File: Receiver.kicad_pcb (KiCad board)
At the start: 2 copper layers, 30 x 30 mm, 25 parts, among them U1 TL074 (ggf. durch TLV4172IPWR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

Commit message: Update schematic and pcb
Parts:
- added D3: LED, LEDs:LED_0603, F.Cu at (127.5, 118.5)
- added D4: LED, LEDs:LED_0603, F.Cu at (90.0, 119.0)
- added J1: +12V, optoreceiver:Hirschmann_MST201, F.Cu at (127.5, 127.5)
- added J2: -12V, optoreceiver:Hirschmann_MST201, F.Cu at (90.0, 127.5)
- added J3: GND, optoreceiver:Hirschmann_MST201, F.Cu at (90.0, 90.0)
- added J4: OUTPUT, optoreceiver:Hirschmann_MST201, F.Cu at (127.5, 90.0)
- added J5: Conn_01x04, Pin_Headers:Pin_Header_Straight_1x04_Pitch2.54mm, F.Cu at (113.0, 127.5)
- added R13: 1k, Resistors_SMD:R_0603, F.Cu at (127.5, 122.0)
- added R14: 1k, Resistors_SMD:R_0603, F.Cu at (90.0, 122.3)
- D2: value Schottky -> BAT54; footprint Diode_SMD:D_SOD-123 -> Diodes_SMD:D_SOT-23_ANK
- moved C1 33.0 mm to (108.5, 107.5)
- moved D2 25.9 mm to (123.0, 113.0)
- moved C2 25.0 mm to (108.5, 104.5)
- moved RV2 20.5 mm to (120.0, 103.0)
- moved D1 19.8 mm to (112.0, 94.5)
- moved RV1 18.5 mm to (99.0, 103.0)
- moved C3 18.2 mm to (102.5, 115.5)
- moved C4 18.2 mm to (102.5, 113.5)
- moved C5 18.2 mm to (114.8, 113.5)
- moved C6 18.2 mm to (114.8, 115.5)
- moved C7 18.2 mm to (114.8, 108.5)
- moved C8 18.2 mm to (119.2, 108.5)
- moved R1 18.2 mm to (99.5, 109.5)
- moved R10 18.2 mm to (116.5, 112.8)
- moved R11 18.2 mm to (116.5, 110.8)
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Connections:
- net Net-(C8-Pad2) renamed /OUTPUT
- U1 pad 4: Net-(U1-Pad4) -> +12V
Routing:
- net Net-(C4-Pad1): track 5.45 -> 0.00 mm
- net Net-(R4-Pad1): track 5.43 -> 0.00 mm
- net Net-(R1-Pad2): track 5.18 -> 0.00 mm
- net Net-(C3-Pad1): track 2.36 -> 0.00 mm, vias 1 -> 0
- added copper zone on B.Cu, net GND
- added copper zone on F.Cu, net GND
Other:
- board size 30 x 30 mm -> 43.5 x 43.5 mm
- board text added: "+12 V"
- board text added: "-12 V"
- board text added: "GND"
- board text added: "OUTPUT"

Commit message: Add files via upload
- Platzierung und Silkscreen angepasst
- 3D Modelle ergänzt
- aktuelle Renderbilder erzeugt
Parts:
- C1, C2, R1, R10, R13, R14, R2, R3, R9: moved to B.Cu
- C5, C6: moved to F.Cu
- D1: footprint kicadlibs:Osram_DIL2_4.3x4.65mm_P5.08mm -> OptoDevice:Osram_SMD2_4.3x4.65mm_P5.08mm
- RV1, RV2: footprint SparkFun-Electromechanical:TRIM_POT -> User-Submitted:BOURNS-3362P_pot
- U1: footprint Package_SO:TSSOP-14_4.4x5mm_P0.65mm -> Package_SO:SOIC-14_3.9x8.7mm_P1.27mm
- moved R6 10.9 mm to (117.0, 117.0)
- moved C7 9.10 mm to (123.5, 111.0), turned to 0 degrees
- moved C2 7.50 mm to (108.5, 112.0)
- moved D1 4.61 mm to (111.0, 90.0)
- moved D3 4.30 mm to (127.5, 122.8), turned to 90 degrees
- moved D4 3.90 mm to (90.0, 122.9), turned to 270 degrees
- moved R5 3.73 mm to (99.5, 116.0)
- moved C8 3.58 mm to (116.0, 107.0), turned to 0 degrees
- moved C3 3.04 mm to (99.5, 116.0)
- moved C4 3.04 mm to (99.5, 113.0)
- moved C6 3.01 mm to (117.0, 113.5), turned to 0 degrees
- moved R8 3.01 mm to (114.5, 114.5), turned to 270 degrees
- moved C5 2.85 mm to (117.0, 115.2), turned to 0 degrees
- moved RV2 2.83 mm to (118.0, 101.0), turned to 0 degrees
- moved R2 2.69 mm to (97.0, 114.5), turned to 270 degrees
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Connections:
- U1 pad 11: Net-(U1-Pad11) -> -12V
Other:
- outline, holes or cut-outs redrawn
- board text added: "+12V"
- board text added: "-12V"
- board text added: "Bandpass Stufe 1"
- board text added: "Bandpass Stufe 2"
- board text added: "Gleichrichter"
- board text added: "NEG PWR"
- board text added: "OUT"
- board text added: "OptoReceiver V0.1"
- board text added: "POS PWR"
- board text added: "Transimpedanz Verstärker"
- board text added: "Verstärker Endstufe"

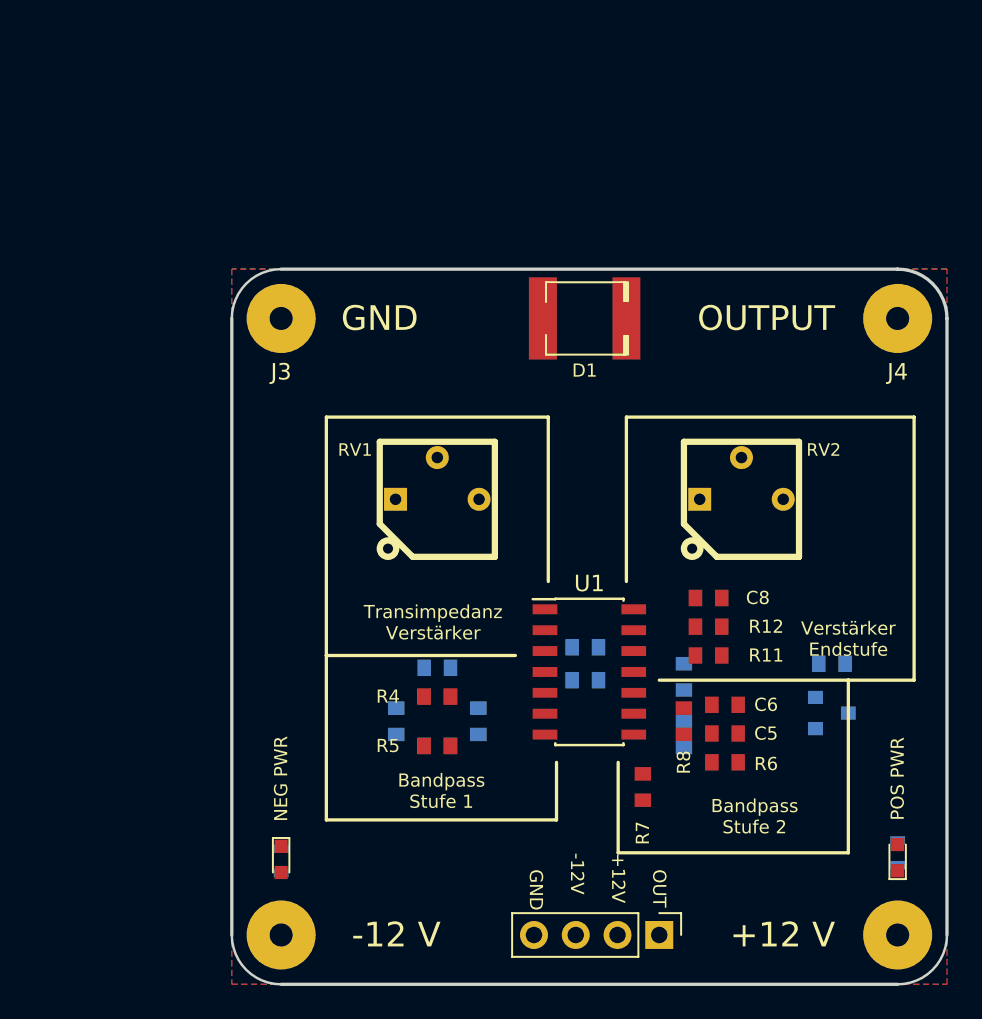
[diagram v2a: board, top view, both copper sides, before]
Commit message: PCB auf Rastermaß angepasst
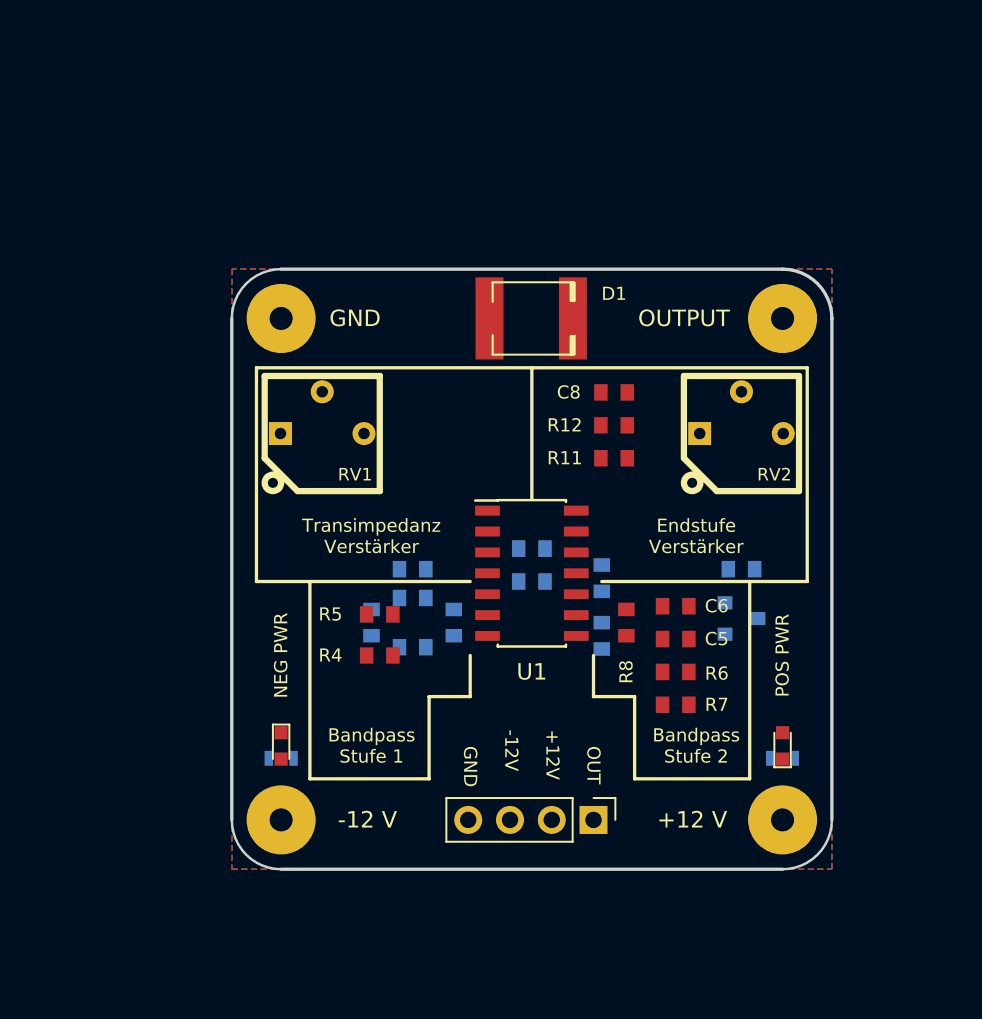
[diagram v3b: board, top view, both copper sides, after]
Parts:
- moved C8 13.8 mm to (110.2, 94.5)
- moved R12 13.5 mm to (110.2, 96.5)
- moved R11 13.3 mm to (110.2, 98.5), turned to 180 degrees
- moved J1 9.90 mm to (120.5, 120.5)
- moved D3 9.76 mm to (120.5, 116.0)
- moved R13 9.06 mm to (120.5, 116.8), turned to 180 degrees
- moved R5 8.73 mm to (96.0, 108.0), turned to 180 degrees
- moved J5 8.06 mm to (109.0, 120.5)
- moved RV1 8.06 mm to (92.5, 97.0)
- moved C7 7.96 mm to (118.0, 105.2)
- moved D2 7.96 mm to (118.0, 108.2)
- moved R10 7.81 mm to (109.5, 105.8)
- moved R9 7.81 mm to (109.5, 109.3)
- moved J2 7.00 mm to (90.0, 120.5)
- moved J4 7.00 mm to (120.5, 90.0)
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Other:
- board size 43.5 x 43.5 mm -> 36.5 x 36.5 mm
- board text added: "Endstufe Verstärker"
- board text added: "OptoReceiver V0.2"
- board text added: "Thomas Gatzweiler"
- board text added: "Tobias Cronenbroeck"
- board text removed: "OptoReceiver V0.1"
- board text removed: "Verstärker Endstufe"

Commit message: Routing + Render Bilder erneuert
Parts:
- moved J5 1.50 mm to (109.0, 119.0)
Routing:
- net +12V: track 0.00 -> 53.9 mm, vias 0 -> 2
- net /OUTPUT: track 0.00 -> 53.6 mm
- net -12V: track 0.00 -> 39.6 mm, vias 0 -> 2
- net Net-(D1-Pad2): track 0.00 -> 27.5 mm
- net Net-(C3-Pad1): track 0.00 -> 20.3 mm, vias 0 -> 1
- net Net-(R1-Pad2): track 0.00 -> 19.1 mm, vias 0 -> 1
- net Net-(C7-Pad2): track 0.00 -> 17.0 mm, vias 0 -> 1
- net Net-(R11-Pad1): track 0.00 -> 16.3 mm
- net Net-(C5-Pad1): track 0.00 -> 13.2 mm, vias 0 -> 1
- net Net-(R12-Pad1): track 0.00 -> 12.7 mm, vias 0 -> 1
- net Net-(R4-Pad1): track 0.00 -> 12.2 mm
- net Net-(R10-Pad2): track 0.00 -> 6.72 mm, vias 0 -> 1
- net Net-(C3-Pad2): track 0.00 -> 6.66 mm
- net Net-(C5-Pad2): track 0.00 -> 6.00 mm
- net Net-(C6-Pad1): track 0.00 -> 5.47 mm
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
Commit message: Real Value Simulation + Update in Schematic
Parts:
- C3, C4: value 390p -> 750p
- C5, C6: value 390p -> 820p
- R1: value 75K -> 24K
- R10: value 274 -> 360
- R2: value 1K02 -> 1K
- R3: value 102K -> 100K
- R4: value 15K4 -> 22K
- R5: value 249 -> 360
- R6: value 49K9 -> 24K
- R7: value 976 -> 1K
- R8: value 97K6 -> 100K
- R9: value 15K -> 22K
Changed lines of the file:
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@@
     (35 F.Paste user)
     (36 B.SilkS user)
-    (37 F.SilkS user)
+    (37 F.SilkS user hide)
     (38 B.Mask user)
-    (39 F.Mask user)
+    (39 F.Mask user hide)
     (40 Dwgs.User user)
     (41 Cmts.User user)
@@
     (45 Margin user)
     (46 B.CrtYd user)
-    (47 F.CrtYd user)
+    (47 F.CrtYd user hide)
     (48 B.Fab user)
-    (49 F.Fab user)
+    (49 F.Fab user hide)
   )
   (setup
-    (last_trace_width 0.5)
+    (last_trace_width 0.25)
     (user_trace_width 0.3)
     (user_trace_width 0.5)
@@
       (effects (font (size 0.8 0.8) (thickness 0.15)) (justify mirror))
     )
-    (fp_text value 390p (at 0 -1.45 180) (layer B.Fab)
+    (fp_text value 750p (at 0 -1.45 180) (layer B.Fab)
       (effects (font (size 0.8 0.8) (thickness 0.15)) (justify mirror))
     )
@@
       (effects (font (size 0.8 0.8) (thickness 0.15)) (justify mirror))
     )
-    (fp_text value 390p (at 0 -1.45 180) (layer B.Fab)
+    (fp_text value 750p (at 0 -1.45 180) (layer B.Fab)
       (effects (font (size 0.8 0.8) (thickness 0.15)) (justify mirror))
     )
@@
       (effects (font (size 0.8 0.8) (thickness 0.15)))
     )
-    (fp_text value 390p (at 0 1.45) (layer F.Fab)
+    (fp_text value 820p (at 0 1.45) (layer F.Fab)
       (effects (font (size 0.8 0.8) (thickness 0.15)))
     )
@@
       (effects (font (size 0.8 0.8) (thickness 0.15)))
     )
-    (fp_text value 390p (at 0 1.45) (layer F.Fab)
+    (fp_text value 820p (at 0 1.45) (layer F.Fab)
       (effects (font (size 0.8 0.8) (thickness 0.15)))
     )
@@
       (effects (font (size 0.8 0.8) (thickness 0.15)) (justify mirror))
     )
-    (fp_text value 75K (at 0 -1.45) (layer B.Fab)
+    (fp_text value 24K (at 0 -1.45) (layer B.Fab)
       (effects (font (size 0.8 0.8) (thickness 0.15)) (justify mirror))
     )
@@
       (effects (font (size 0.8 0.8) (thickness 0.15)) (justify mirror))
     )
-    (fp_text value 1K02 (at 0 -1.45 270) (layer B.Fab)
+    (fp_text value 1K (at 0 -1.45 270) (layer B.Fab)
       (effects (font (size 0.8 0.8) (thickness 0.15)) (justify mirror))
     )
@@
       (effects (font (size 0.8 0.8) (thickness 0.15)) (justify mirror))
     )
-    (fp_text value 102K (at 0 -1.45 270) (layer B.Fab)
+    (fp_text value 100K (at 0 -1.45 270) (layer B.Fab)
       (effects (font (size 0.8 0.8) (thickness 0.15)) (justify mirror))
     )
@@
       (effects (font (size 0.8 0.8) (thickness 0.15)))
     )
-    (fp_text value 15K4 (at 0 1.45) (layer F.Fab)
+    (fp_text value 22K (at 0 1.45) (layer F.Fab)
       (effects (font (size 0.8 0.8) (thickness 0.15)))
     )
@@
       (effects (font (size 0.8 0.8) (thickness 0.15)))
     )
-    (fp_text value 249 (at 0 1.45 180) (layer F.Fab)
+    (fp_text value 360 (at 0 1.45 180) (layer F.Fab)
       (effects (font (size 0.8 0.8) (thickness 0.15)))
     )
@@
       (effects (font (size 0.8 0.8) (thickness 0.15)))
     )
-    (fp_text value 49K9 (at 0 1.45 180) (layer F.Fab)
+    (fp_text value 24K (at 0 1.45 180) (layer F.Fab)
       (effects (font (size 0.8 0.8) (thickness 0.15)))
     )
@@
       (effects (font (size 0.8 0.8) (thickness 0.15)))
     )
-    (fp_text value 976 (at 0 1.45) (layer F.Fab)
+    (fp_text value 1K (at 0 1.45) (layer F.Fab)
       (effects (font (size 0.8 0.8) (thickness 0.15)))
     )
@@
       (effects (font (size 0.8 0.8) (thickness 0.15)))
     )
-    (fp_text value 97K6 (at 0 1.45 270) (layer F.Fab)
+    (fp_text value 100K (at 0 1.45 270) (layer F.Fab)
       (effects (font (size 0.8 0.8) (thickness 0.15)))
     )
@@
       (effects (font (size 0.8 0.8) (thickness 0.15)) (justify mirror))
     )
-    (fp_text value 15K (at 0 -1.45 270) (layer B.Fab)
+    (fp_text value 22K (at 0 -1.45 270) (layer B.Fab)
       (effects (font (size 0.8 0.8) (thickness 0.15)) (justify mirror))
     )
@@
       (effects (font (size 0.8 0.8) (thickness 0.15)) (justify mirror))
     )
-    (fp_text value 274 (at 0 -1.45 270) (layer B.Fab)
-      (effects (font (size 0.8 0.8) (thickness 0.15)) (justify mirror))
-    )
+    (fp_text value 360 (at 0 -1.45 270) (layer B.Fab)
+      (effects (font (size 0.8 0.8) (thickness 0.15)) (justify mirror))
+    )
